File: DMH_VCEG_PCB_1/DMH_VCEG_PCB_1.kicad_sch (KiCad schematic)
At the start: 0 parts

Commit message: Initiated schematic design
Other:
- sheet Core Circuit renamed Core Circuit A
- sheet Inputs and Outputs renamed Inputs and Outputs A
- added sheet Inputs and Outputs B (Inputs_and_Outputs_B.kicad_sch)
- sheet Core Circuit A: file Core_Circuit.kicad_sch -> Core_Circuit_A.kicad_sch
- sheet Inputs and Outputs A: file Inputs_and_Outputs.kicad_sch -> Inputs_and_Outputs_A.kicad_sch
- sheet Power ports: added none; removed Bus Gate
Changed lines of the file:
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@@
-			)
-		)
-		(pin "Bus Gate" output
-			(at 127 96.52 180)
-			(effects
-				(font
-					(size 1.27 1.27)
-				)
-				(justify left)
 			)
 		)
@@
 		)
 		(instances
-			(project "DMH-Kosmo-10cm-PCB"
+			(project "DMH_VCEG_PCB_1"
 				(path "/58f4306d-5387-4983-bb08-41a2313fd315"
 					(page "4")
@@
 	)
 	(sheet
-		(at 63.5 76.2)
+		(at 25.4 114.3)
+		(size 25.4 50.8)
+		(exclude_from_sim no)
+		(in_bom yes)
+		(on_board yes)
+		(dnp no)
+		(fields_autoplaced yes)
+		(stroke
+			(width 0.1524)
+			(type solid)
+		)
+		(fill
+			(color 0 0 0 0.0000)
+		)
+		(property "Sheetname" "Inputs and Outputs B"
+			(at 25.4 113.5884 0)
+			(effects
+				(font
+					(size 1.27 1.27)
+				)
+				(justify left bottom)
+			)
+		)
+		(property "Sheetfile" "Inputs_and_Outputs_B.kicad_sch"
+			(at 25.4 165.6846 0)
+			(effects
+				(font
+					(size 1.27 1.27)
+				)
+				(justify left top)
+				(hide yes)
+			)
+		)
+		(instances
+			(project "DMH_VCEG_PCB_1"
+				(path "/58f4306d-5387-4983-bb08-41a2313fd315"
+					(page "3")
+				)
+			)
+		)
+	)
+	(sheet
+		(at 63.5 38.1)
 		(size 50.8 50.8)
 		(exclude_from_sim no)
@@
 			(color 0 0 0 0.0000)
 		)
-		(property "Sheetname" "Core Circuit"
-			(at 63.5 75.4884 0)
+		(property "Sheetname" "Core Circuit A"
+			(at 63.5 37.3884 0)
 			(effects
 				(font
@@
 			)
 		)
-		(property "Sheetfile" "Core_Circuit.kicad_sch"
-			(at 63.5 127.5846 0)
+		(property "Sheetfile" "Core_Circuit_A.kicad_sch"
+			(at 63.5 89.4846 0)
 			(effects
 				(font
@@
 		)
 		(instances
-			(project "DMH-Kosmo-10cm-PCB"
+			(project "DMH_VCEG_PCB_1"
 				(path "/58f4306d-5387-4983-bb08-41a2313fd315"
-					(page "3")
+					(page "4")
 				)
 			)
@@
 	)
 	(sheet
-		(at 25.4 76.2)
+		(at 25.4 38.1)
 		(size 25.4 50.8)
 		(exclude_from_sim no)
@@
 			(color 0 0 0 0.0000)
 		)
-		(property "Sheetname" "Inputs and Outputs"
-			(at 25.4 75.4884 0)
+		(property "Sheetname" "Inputs and Outputs A"
+			(at 25.4 37.3884 0)
 			(effects
 				(font
@@
 			)
 		)
-		(property "Sheetfile" "Inputs_and_Outputs.kicad_sch"
-			(at 25.4 127.5846 0)
+		(property "Sheetfile" "Inputs_and_Outputs_A.kicad_sch"
+			(at 25.4 89.4846 0)
 			(effects
 				(font
@@
 		)
 		(instances
-			(project "DMH-Kosmo-10cm-PCB"
+			(project "DMH_VCEG_PCB_1"
 				(path "/58f4306d-5387-4983-bb08-41a2313fd315"
 					(page "2")

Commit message: IO pages done
Core Circuit A ongoing
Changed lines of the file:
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@@
 	(sheet
 		(at 25.4 114.3)
-		(size 25.4 50.8)
+		(size 25.4 63.5)
 		(exclude_from_sim no)
 		(in_bom yes)
@@
 		)
 		(property "Sheetfile" "Inputs_and_Outputs_B.kicad_sch"
-			(at 25.4 165.6846 0)
+			(at 25.4 178.3846 0)
 			(effects
 				(font
@@
 	(sheet
 		(at 25.4 38.1)
-		(size 25.4 50.8)
+		(size 25.4 63.5)
 		(exclude_from_sim no)
 		(in_bom yes)
@@
 		)
 		(property "Sheetfile" "Inputs_and_Outputs_A.kicad_sch"
-			(at 25.4 89.4846 0)
+			(at 25.4 102.1846 0)
 			(effects
 				(font

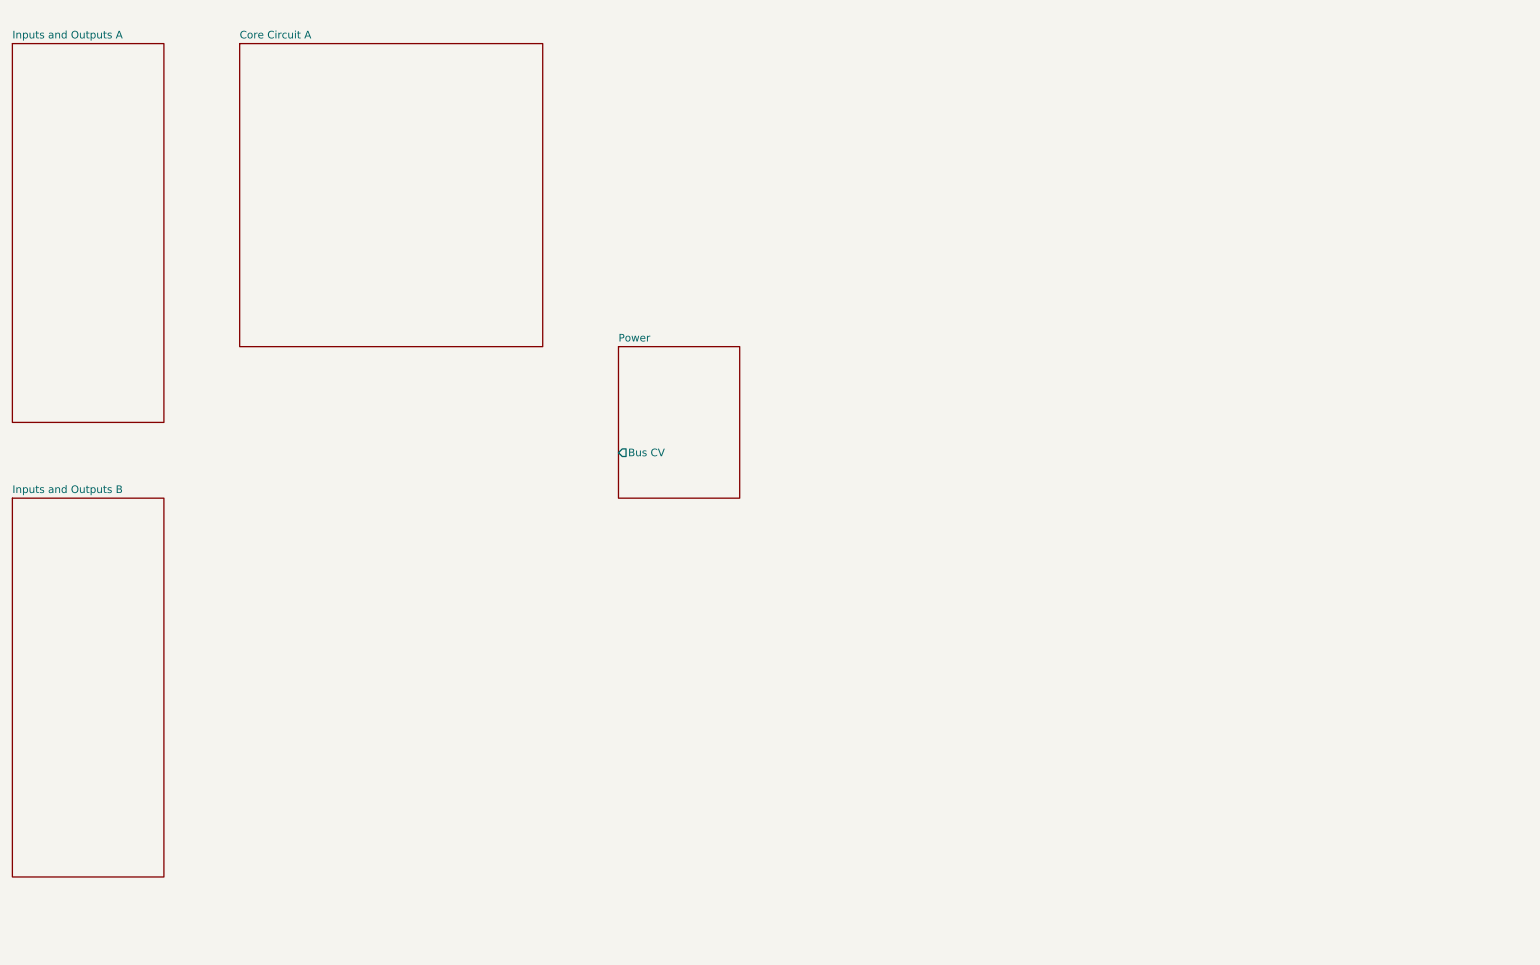
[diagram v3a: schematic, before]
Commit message: Core Circuit A ready for breadboarding
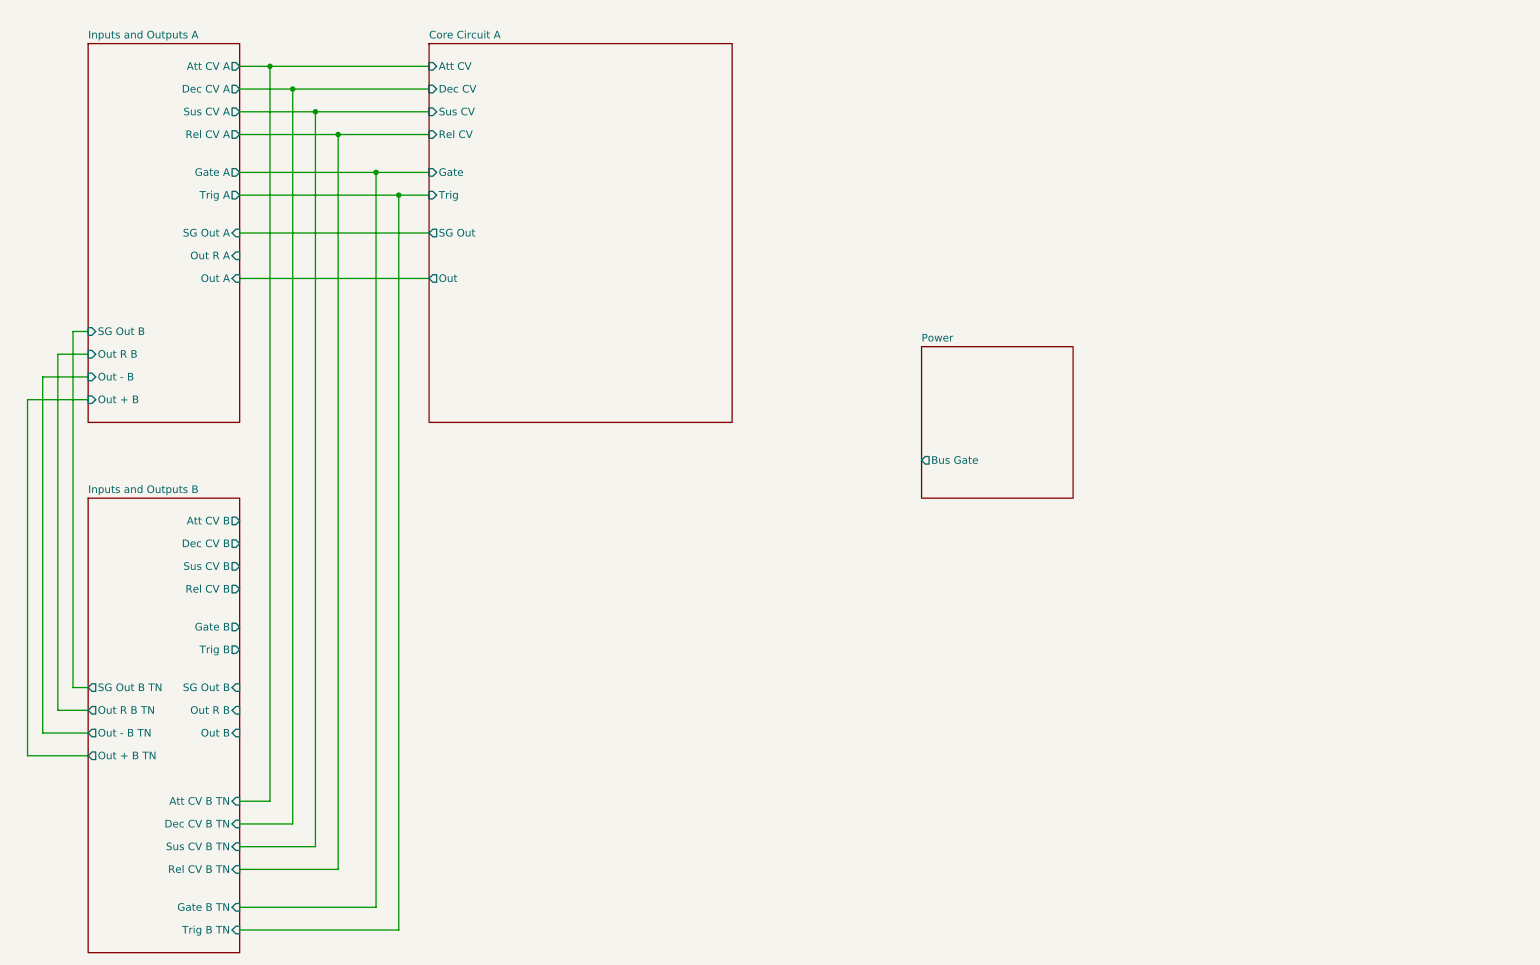
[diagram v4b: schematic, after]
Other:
- sheet Core Circuit A ports: added Att CV, Dec CV, Gate, Out, Rel CV, SG Out, Sus CV, Trig; removed none
- sheet Inputs and Outputs A ports: added Att CV A, Dec CV A, Gate A, Out + B, Out - B, Out A, Out R A, Out R B, Rel CV A, SG Out A, SG Out B, Sus CV A, Trig A; removed none
- sheet Inputs and Outputs B ports: added Att CV B, Att CV B TN, Dec CV B, Dec CV B TN, Gate B, Gate B TN, Out + B TN, Out - B TN, Out B, Out R B, Out R B TN, Rel CV B, Rel CV B TN, SG Out B, SG Out B TN, Sus CV B, Sus CV B TN, Trig B, Trig B TN; removed none
- sheet Power ports: added Bus Gate; removed Bus CV

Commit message: MFOS based core circuit in progress
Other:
- added sheet Envylope A (Envylope_A.kicad_sch)
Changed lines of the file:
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@@
 		(comment 1 "PCB for 15cm Kosmo format synthesizer module")
 	)
-	(junction
-		(at 86.36 59.69)
-		(diameter 0)
-		(color 0 0 0 0)
-	)
-	(junction
-		(at 72.39 45.72)
-		(diameter 0)
-		(color 0 0 0 0)
-	)
-	(junction
-		(at 76.2 49.53)
-		(diameter 0)
-		(color 0 0 0 0)
-	)
-	(junction
-		(at 68.58 41.91)
-		(diameter 0)
-		(color 0 0 0 0)
-	)
-	(junction
-		(at 80.01 53.34)
-		(diameter 0)
-		(color 0 0 0 0)
-	)
-	(junction
-		(at 90.17 63.5)
-		(diameter 0)
-		(color 0 0 0 0)
-	)
 	(wire
 		(pts
@@
 	(wire
 		(pts
-			(xy 80.01 53.34) (xy 95.25 53.34)
-		)
-		(stroke
-			(width 0)
-			(type default)
-		)
-	)
-	(wire
-		(pts
 			(xy 63.5 186.69) (xy 90.17 186.69)
 		)
@@
 	(wire
 		(pts
-			(xy 72.39 45.72) (xy 95.25 45.72)
-		)
-		(stroke
-			(width 0)
-			(type default)
-		)
-	)
-	(wire
-		(pts
 			(xy 63.5 168.91) (xy 72.39 168.91)
 		)
@@
 	(wire
 		(pts
-			(xy 76.2 49.53) (xy 95.25 49.53)
-		)
-		(stroke
-			(width 0)
-			(type default)
-		)
-	)
-	(wire
-		(pts
-			(xy 68.58 41.91) (xy 95.25 41.91)
-		)
-		(stroke
-			(width 0)
-			(type default)
-		)
-	)
-	(wire
-		(pts
-			(xy 86.36 59.69) (xy 95.25 59.69)
-		)
-		(stroke
-			(width 0)
-			(type default)
-		)
-	)
-	(wire
-		(pts
 			(xy 68.58 41.91) (xy 68.58 165.1)
 		)
@@
 	(wire
 		(pts
-			(xy 63.5 69.85) (xy 95.25 69.85)
-		)
-		(stroke
-			(width 0)
-			(type default)
-		)
-	)
-	(wire
-		(pts
 			(xy 38.1 146.05) (xy 35.56 146.05)
 		)
@@
 	(wire
 		(pts
-			(xy 90.17 63.5) (xy 95.25 63.5)
-		)
-		(stroke
-			(width 0)
-			(type default)
-		)
-	)
-	(wire
-		(pts
 			(xy 63.5 45.72) (xy 72.39 45.72)
 		)
@@
 		)
 	)
-	(wire
-		(pts
-			(xy 63.5 77.47) (xy 95.25 77.47)
-		)
-		(stroke
-			(width 0)
-			(type default)
-		)
-	)
 	(sheet
-		(at 177.8 88.9)
+		(at 242.57 132.08)
 		(size 25.4 25.4)
 		(exclude_from_sim no)
@@
 		)
 		(property "Sheetname" "Power"
-			(at 177.8 88.1884 0)
+			(at 242.57 131.3684 0)
 			(effects
 				(font
@@
 		)
 		(property "Sheetfile" "Power.kicad_sch"
-			(at 177.8 114.8846 0)
+			(at 242.57 158.0646 0)
 			(effects
 				(font
@@
 		)
 		(pin "Bus Gate" output
-			(at 177.8 107.95 180)
+			(at 242.57 151.13 180)
 			(effects
 				(font
@@
 	)
 	(sheet
-		(at 95.25 38.1)
+		(at 208.28 35.56)
 		(size 50.8 63.5)
 		(exclude_from_sim no)
@@
 			(color 0 0 0 0.0000)
 		)
-		(property "Sheetname" "Core Circuit A"
-			(at 95.25 37.3884 0)
+		(property "Sheetname" "Envylope A"
+			(at 208.28 34.8484 0)
 			(effects
 				(font
@@
 			)
 		)
-		(property "Sheetfile" "Core_Circuit_A.kicad_sch"
-			(at 95.25 102.1846 0)
+		(property "Sheetfile" "Envylope_A.kicad_sch"
+			(at 208.28 99.6446 0)
 			(effects
 				(font
@@
 		)
 		(pin "Att CV" input
-			(at 95.25 41.91 180)
+			(at 208.28 39.37 180)
 			(effects
 				(font
@@
 		)
 		(pin "Dec CV" input
-			(at 95.25 45.72 180)
+			(at 208.28 43.18 180)
 			(effects
 				(font
@@
 		)
 		(pin "Gate" input
-			(at 95.25 59.69 180)
+			(at 208.28 57.15 180)
 			(effects
 				(font
@@
 		)
 		(pin "Rel CV" input
-			(at 95.25 53.34 180)
+			(at 208.28 50.8 180)
 			(effects
 				(font
@@
 		)
 		(pin "SG Out" output
-			(at 95.25 69.85 180)
+			(at 208.28 67.31 180)
 			(effects
 				(font
@@
 		)
 		(pin "Sus CV" input
-			(at 95.25 49.53 180)
+			(at 208.28 46.99 180)
 			(effects
 				(font
@@
 		)
 		(pin "Trig" input
-			(at 95.25 63.5 180)
+			(at 208.28 60.96 180)
 			(effects
 				(font
@@
 		)
 		(pin "Out" output
-			(at 95.25 77.47 180)
+			(at 208.28 74.93 180)
 			(effects
 				(font
@@
 				)
 			)
+		)
+	)
+	(sheet
+		(at 101.6 38.1)
+		(size 50.8 63.5)
+		(exclude_from_sim no)
+		(in_bom yes)
+		(on_board yes)
+		(dnp no)
+		(fields_autoplaced yes)
+		(stroke
+			(width 0.1524)
+			(type solid)
+		)
+		(fill
+			(color 0 0 0 0.0000)
+		)
+		(property "Sheetname" "Core Circuit A"
+			(at 101.6 37.3884 0)
+			(effects
+				(font
+					(size 1.27 1.27)
+				)
+				(justify left bottom)
+			)
+		)
+		(property "Sheetfile" "Core_Circuit_A.kicad_sch"
+			(at 101.6 102.1846 0)
+			(effects
+				(font
+					(size 1.27 1.27)
+				)
+				(justify left top)
+				(hide yes)
+			)
+		)
+		(pin "Att CV" input
+			(at 101.6 41.91 180)
+			(effects
+				(font
+					(size 1.27 1.27)
+				)
+				(justify left)
+			)
+		)
+		(pin "Dec CV" input
+			(at 101.6 45.72 180)
+			(effects
+				(font
+					(size 1.27 1.27)
+				)
+				(justify left)
+			)
+		)
+		(pin "Gate" input
+			(at 101.6 59.69 180)
+			(effects
+				(font
+					(size 1.27 1.27)
+				)
+				(justify left)
+			)
+		)
+		(pin "Rel CV" input
+			(at 101.6 53.34 180)
+			(effects
+				(font
+					(size 1.27 1.27)
+				)
+				(justify left)
+			)
+		)
+		(pin "SG Out" output
+			(at 101.6 69.85 180)
+			(effects
+				(font
+					(size 1.27 1.27)
+				)
+				(justify left)
+			)
+		)
+		(pin "Sus CV" input
+			(at 101.6 49.53 180)
+			(effects
+				(font
+					(size 1.27 1.27)
+				)
+				(justify left)
+			)
+		)
+		(pin "Trig" input
+			(at 101.6 63.5 180)
+			(effects
+				(font
+					(size 1.27 1.27)
+				)
+				(justify left)
+			)
+		)
+		(pin "Out" output
+			(at 101.6 77.47 180)
+			(effects
+				(font
+					(size 1.27 1.27)
+				)
+				(justify left)
+			)
+		)
+		(instances
+			(project "DMH_VCEG_PCB_1"
+				(path "/58f4306d-5387-4983-bb08-41a2313fd315"
+					(page "5")
+				)
+			)
